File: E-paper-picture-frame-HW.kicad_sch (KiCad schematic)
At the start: 8 parts

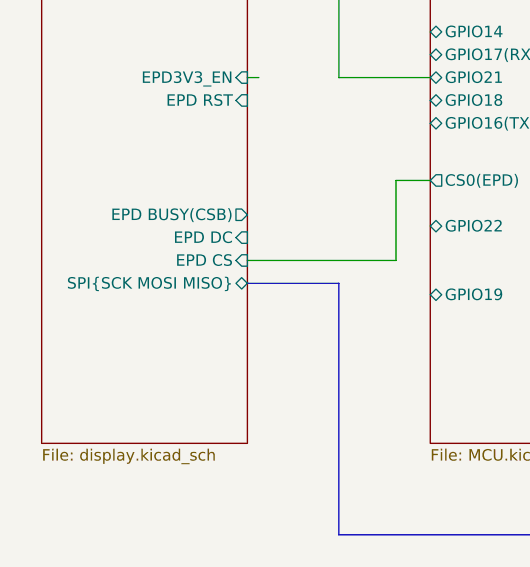
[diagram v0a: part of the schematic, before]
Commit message: Finished USB, SD card and Power Mmt layout
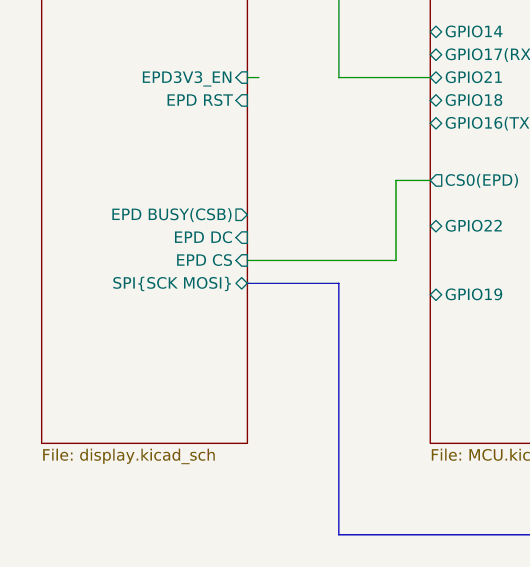
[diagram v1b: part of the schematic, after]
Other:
- sheet Display ports: added SPI{SCK MOSI}; removed SPI{SCK MOSI MISO}
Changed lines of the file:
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@@
 			)
 		)
-		(pin "SPI{SCK MOSI MISO}" bidirectional
+		(pin "SPI{SCK MOSI}" bidirectional
 			(at 93.98 92.71 0)
 			(effects

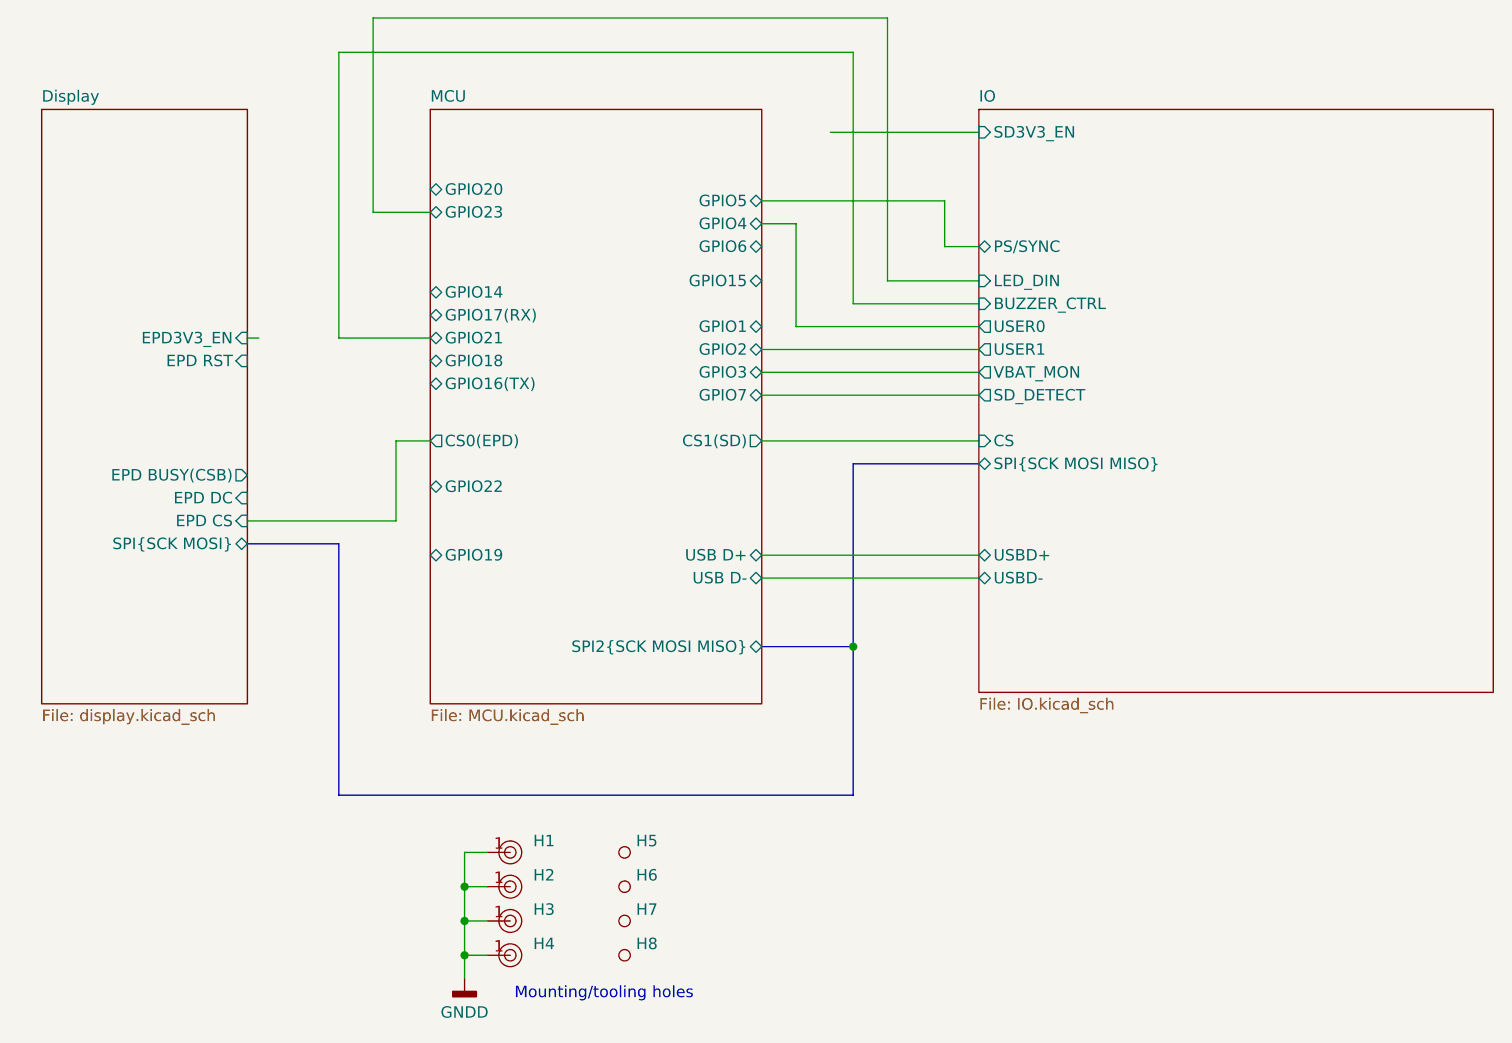
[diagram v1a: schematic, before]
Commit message: First draft of layout done. Needs cleaning and DRC
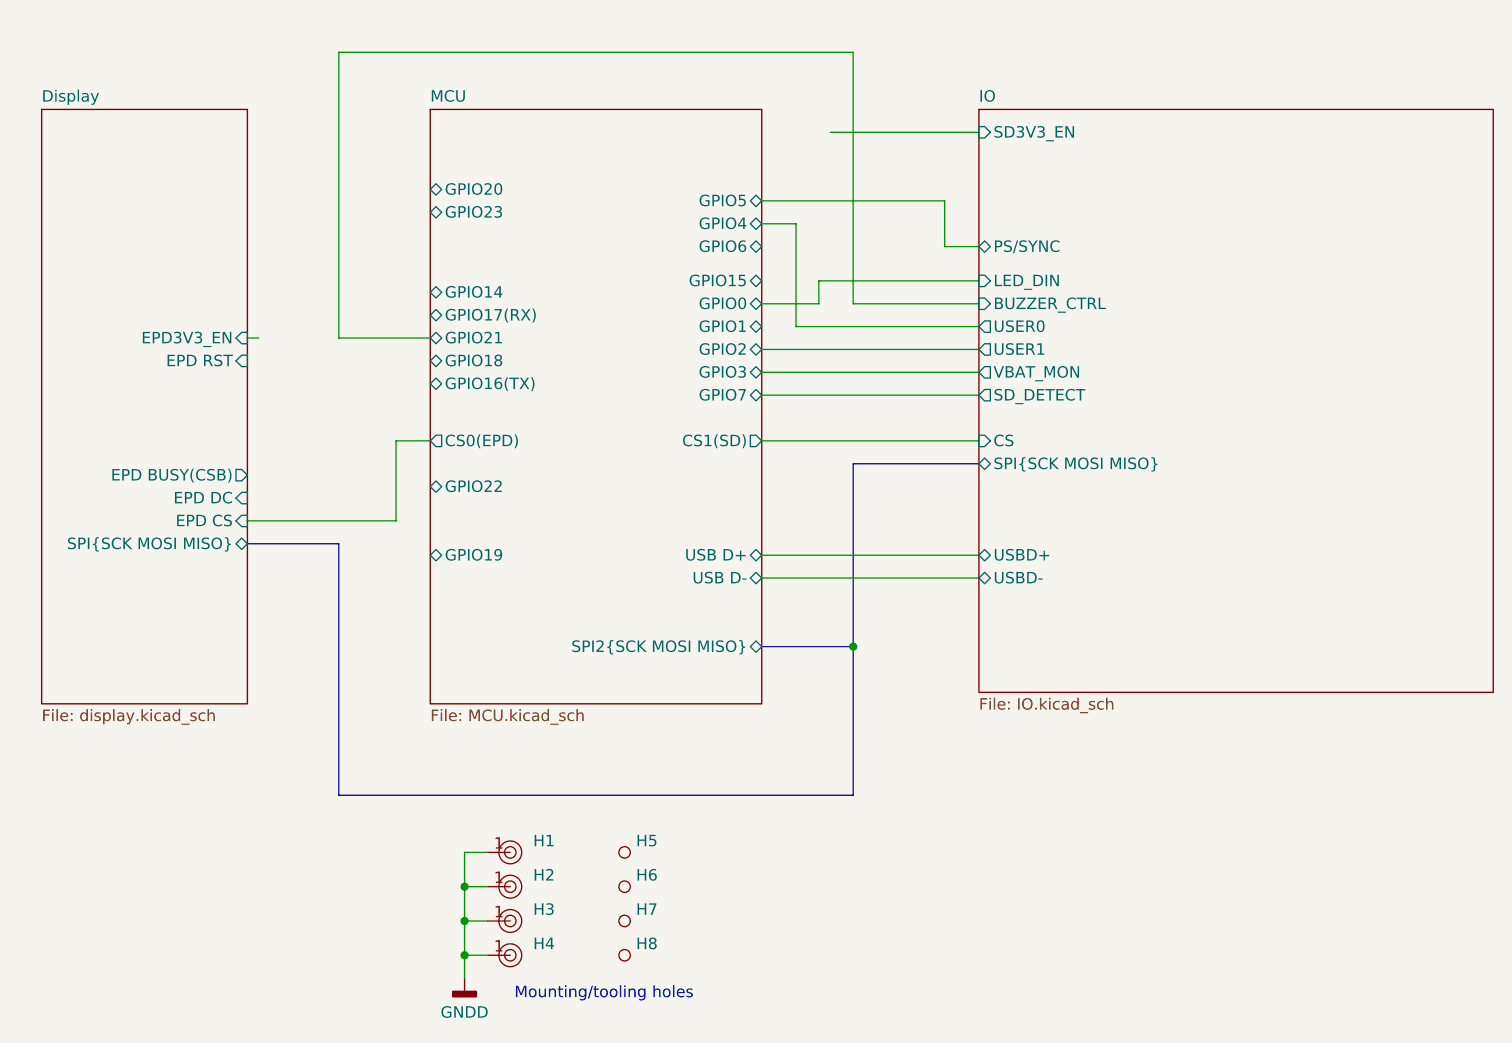
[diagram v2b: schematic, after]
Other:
- sheet Display ports: added SPI{SCK MOSI MISO}; removed SPI{SCK MOSI}
- sheet MCU ports: added GPIO0; removed none
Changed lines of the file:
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@@
 	(wire
 		(pts
-			(xy 165.1 63.5) (xy 175.26 63.5)
+			(xy 175.26 63.5) (xy 157.48 63.5)
 		)
 		(stroke
@@
 	(wire
 		(pts
+			(xy 157.48 66.04) (xy 151.13 66.04)
+		)
+		(stroke
+			(width 0)
+			(type default)
+		)
+	)
+	(wire
+		(pts
 			(xy 151.13 57.15) (xy 154.94 57.15)
 		)
@@
 	(wire
 		(pts
-			(xy 107.95 34.29) (xy 165.1 34.29)
-		)
-		(stroke
-			(width 0)
-			(type default)
-		)
-	)
-	(wire
-		(pts
 			(xy 151.13 93.98) (xy 175.26 93.98)
 		)
@@
 	(wire
 		(pts
-			(xy 165.1 34.29) (xy 165.1 63.5)
-		)
-		(stroke
-			(width 0)
-			(type default)
-		)
-	)
-	(wire
-		(pts
-			(xy 114.3 55.88) (xy 107.95 55.88)
-		)
-		(stroke
-			(width 0)
-			(type default)
-		)
-	)
-	(wire
-		(pts
 			(xy 151.13 96.52) (xy 175.26 96.52)
 		)
@@
 	(wire
 		(pts
-			(xy 107.95 55.88) (xy 107.95 34.29)
-		)
-		(stroke
-			(width 0)
-			(type default)
-		)
-	)
-	(wire
-		(pts
 			(xy 171.45 54.61) (xy 171.45 59.69)
 		)
@@
 		(pts
 			(xy 151.13 81.28) (xy 175.26 81.28)
+		)
+		(stroke
+			(width 0)
+			(type default)
+		)
+	)
+	(wire
+		(pts
+			(xy 157.48 63.5) (xy 157.48 66.04)
 		)
 		(stroke
@@
 			)
 		)
-		(pin "SPI{SCK MOSI}" bidirectional
+		(pin "SPI{SCK MOSI MISO}" bidirectional
 			(at 93.98 92.71 0)
 			(effects
@@
 			(effects
 				(font
+					(size 1.27 1.27)
+				)
+				(justify right)
+			)
+		)
+		(pin "GPIO0" bidirectional
+			(at 151.13 66.04 0)
+			(effects
+				(font
